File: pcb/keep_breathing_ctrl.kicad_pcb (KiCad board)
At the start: 4 copper layers, 131 x 112 mm, 149 parts, among them J1 Barrel_Jack_Switch, J2 Screw_Terminal, P1 CONN_RASPBERRY, Q1 PN2222, Q2 PN2222, U1 MPL3115A2, U10 PCF8523TK, U11 AQH3213AX, U12 AQH3213AX, U13 HTS221, U14 ICE40UP5K-SG48ITR, U15 W25Q32JVSSIM, U16 UCC12040, U17 ISO7762, U2 powerSTEP01, U3 TLP240D, U4 TLP240D, U5 TLP240D, U6 TLP240D, U7 TLP240D, U8 TLP240D, U9 ZLDO1117G33TA

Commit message: stepper planes
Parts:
- C43, C46, C49, C51, C52, C53, R30: moved to B.Cu
- moved C46 168.6 mm to (142.7, 91.4)
- moved C53 144.0 mm to (127.3, 94.7)
- moved C43 143.4 mm to (139.7, 91.9)
- moved C52 140.3 mm to (127.4, 92.7)
- moved U15 138.6 mm to (124.5, 87.9)
- moved C51 137.0 mm to (134.5, 81.4)
- moved C49 135.4 mm to (134.8, 83.5)
- moved R30 133.6 mm to (127.5, 88.7), turned to 180 degrees
- moved R4 9.93 mm to (63.0, 106.6), turned to 90 degrees
- moved C9 7.27 mm to (56.5, 131.0)
- moved C5 6.79 mm to (61.2, 106.6), turned to 90 degrees
- moved C4 0.62 mm to (59.5, 123.3)
- moved C12 0.51 mm to (59.5, 121.5)
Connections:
- C42 pad 1: /SensorShields/+1.2V_CORE -> +1V2
- R32 pad 2: (no net) -> +1V2
- U14 pad 30: /SensorShields/+1.2V_CORE -> +1V2
- U14 pad 5: /SensorShields/+1.2V_CORE -> +1V2
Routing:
- net GND_MOTOR: track 1.65 -> 8.69 mm, vias 42 -> 46
- net SM_ADC: track 16.1 -> 16.7 mm
- net OUTA1: track 6.04 -> 6.29 mm, vias 14 -> 15
- net OUTB1: vias 14 -> 15
- added copper zone on F.Cu, net GND_MOTOR
- added copper zone on In2.Cu, net GND_MOTOR
- added copper zone on F.Cu, net VMOTOR
- added copper zone on In1.Cu, net VMOTOR
- removed copper zone on F.Cu, net GND

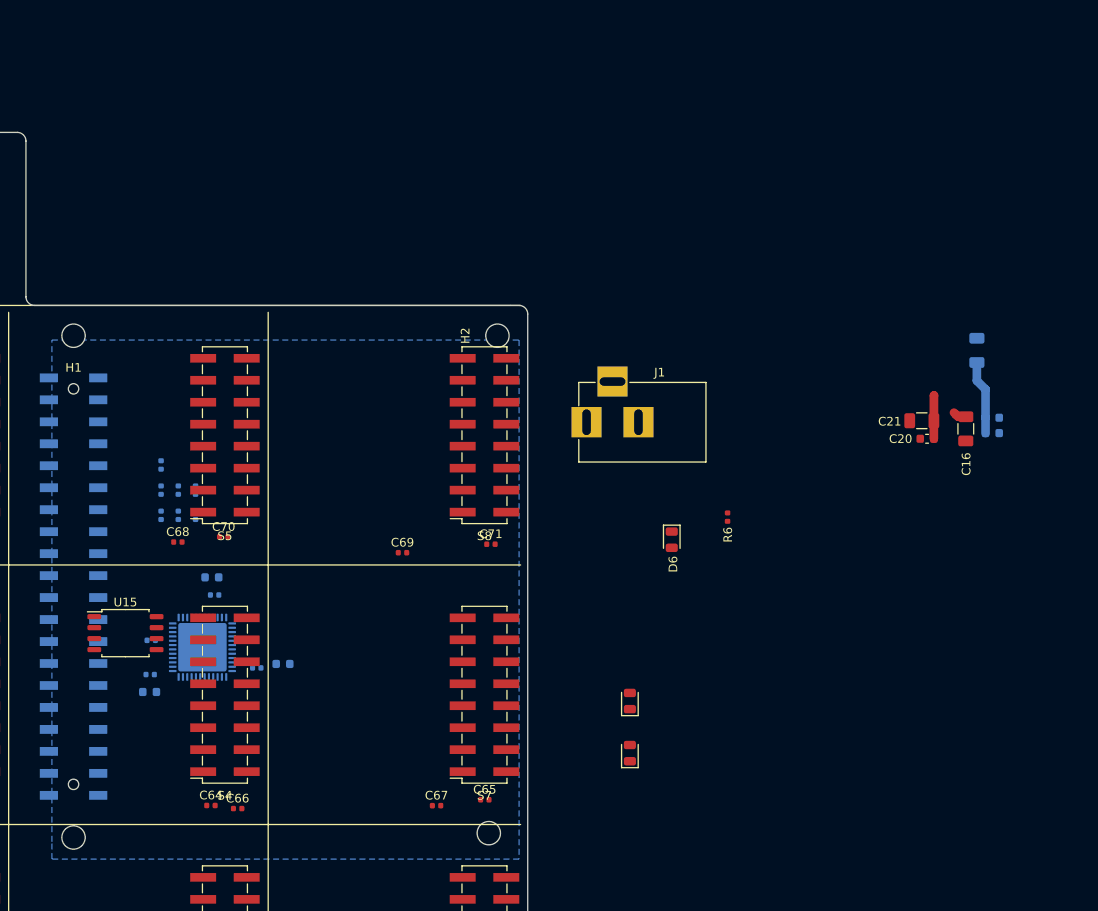
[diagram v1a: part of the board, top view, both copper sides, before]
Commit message: stm32 jtag  connected
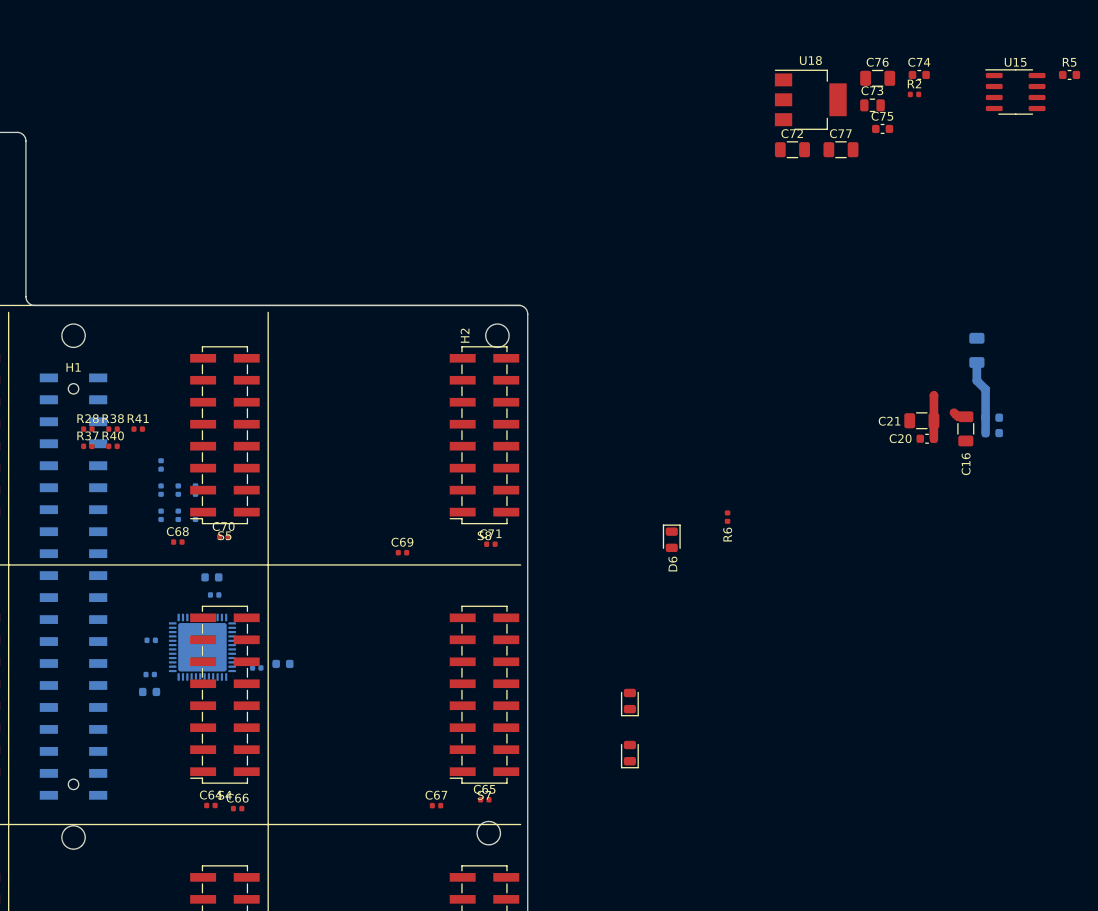
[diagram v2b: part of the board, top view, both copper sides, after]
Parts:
- removed J1: Barrel_Jack_Switch, TH:BARREL_JACK
- added C72: 33u, Capacitor_SMD:C_1206_3216Metric, F.Cu at (201.6, 32.0)
- added C73: 10u, Capacitor_SMD:C_0805_2012Metric, F.Cu at (210.8, 26.9)
- added C74: 0.1u, Capacitor_SMD:C_0603_1608Metric, F.Cu at (216.3, 23.4)
- added C75: 0.1u, Capacitor_SMD:C_0603_1608Metric, F.Cu at (212.0, 29.6)
- added C76: 33u, Capacitor_SMD:C_1206_3216Metric, F.Cu at (211.4, 23.8)
- added C77: 33u, Capacitor_SMD:C_1206_3216Metric, F.Cu at (207.2, 32.0)
- added R2: 120, Resistor_SMD:R_0402_1005Metric, F.Cu at (215.7, 25.6)
- added R28: 100, Resistor_SMD:R_0402_1005Metric, F.Cu at (120.2, 64.3)
- added R37: 100, Resistor_SMD:R_0402_1005Metric, F.Cu at (120.2, 66.3)
- added R38: 100, Resistor_SMD:R_0402_1005Metric, F.Cu at (123.1, 64.3)
- added R40: 100, Resistor_SMD:R_0402_1005Metric, F.Cu at (123.1, 66.3)
- added R41: 100, Resistor_SMD:R_0402_1005Metric, F.Cu at (126.0, 64.3)
- added R5: 10K, Resistor_SMD:R_0603_1608Metric, F.Cu at (233.6, 23.4)
- added U18: ZLDO1117G33TA, SMD:SOT-223, F.Cu at (203.7, 26.2)
- U15: value W25Q32JVSSIM -> GD25Q32CTIGR-Memory_Flash; footprint Package_SO:SOIC-8_5.23x5.23mm_P1.27mm -> Package_SO:SOIC-8_3.9x4.9mm_P1.27mm
- moved U15 120.4 mm to (227.4, 25.3)
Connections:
- net +1V2 renamed 1V2_ICE
- C20 pad 1: 3V3_ESP -> 3V3_STM
- C21 pad 1: 3V3_ESP -> 3V3_STM
- C43 pad 1: +3V3 -> 3V3_ICE
- C44 pad 1: +3V3 -> 3V3_ICE
- C45 pad 1: +3V3 -> 3V3_ICE
- C46 pad 1: +3V3 -> 3V3_ICE
- C49 pad 1: +3V3 -> 3V3_ICE
- C51 pad 1: +3V3 -> 3V3_ICE
- C52 pad 1: +3V3 -> 3V3_ICE
- C53 pad 1: +3V3 -> 3V3_ICE
- P1 pad 12: (no net) -> /Rapsberry/JNRST
- P1 pad 16: (no net) -> /Rapsberry/JTDO
- P1 pad 18: (no net) -> /Rapsberry/JTDI
- P1 pad 19: (no net) -> /Rapsberry/SPI_MOSI
- P1 pad 21: (no net) -> /Rapsberry/SPI_MISO
- P1 pad 22: (no net) -> /Rapsberry/JTCK
- P1 pad 23: (no net) -> /Rapsberry/SPI_CLK
- P1 pad 24: (no net) -> /Rapsberry/SPI_CS
- P1 pad 26: (no net) -> /Rapsberry/JTMS
- P1 pad 29: (no net) -> /Rapsberry/RST_ICE
- R29 pad 2: +3V3 -> 3V3_ICE
- R30 pad 2: +3V3 -> 3V3_ICE
- R31 pad 2: +3V3 -> 3V3_ICE
- R33 pad 2: +3V3 -> 3V3_ICE
- R34 pad 2: +3V3 -> 3V3_ICE
- U14 pad 1: +3V3 -> 3V3_ICE
- U14 pad 14: (no net) -> /SensorShields/FPGA_SO
- U14 pad 17: (no net) -> /SensorShields/FPGA_SI
- U14 pad 22: +3V3 -> 3V3_ICE
- U14 pad 33: +3V3 -> 3V3_ICE
- U15 pad 2: (no net) -> /SensorShields/FPGA_SI
- U15 pad 5: (no net) -> /SensorShields/FPGA_SO
- U15 pad 8: +3V3 -> 3V3_ICE
- U9 pad 2: 3V3_ESP -> 3V3_STM
- U9 pad 4: 3V3_ESP -> 3V3_STM
- UST1 pad 100: +3.3VP -> 3V3_STM
- UST1 pad 11: +3.3VP -> 3V3_STM
- UST1 pad 19: +3.3VP -> 3V3_STM
- UST1 pad 28: +3.3VP -> 3V3_STM
- UST1 pad 50: +3.3VP -> 3V3_STM
- UST1 pad 72: (no net) -> /Rapsberry/JTMS
- UST1 pad 75: +3.3VP -> 3V3_STM
- UST1 pad 76: (no net) -> /Rapsberry/JTCK
- UST1 pad 77: (no net) -> /Rapsberry/JTDI
- UST1 pad 89: (no net) -> /Rapsberry/JTDO
- UST1 pad 90: (no net) -> /Rapsberry/JNRST
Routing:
- net 3V3_STM: track 0.00 -> 5.03 mm
- net 3V3_ESP: track 5.03 -> 0.00 mm
- removed copper zone on B.Cu, net GND

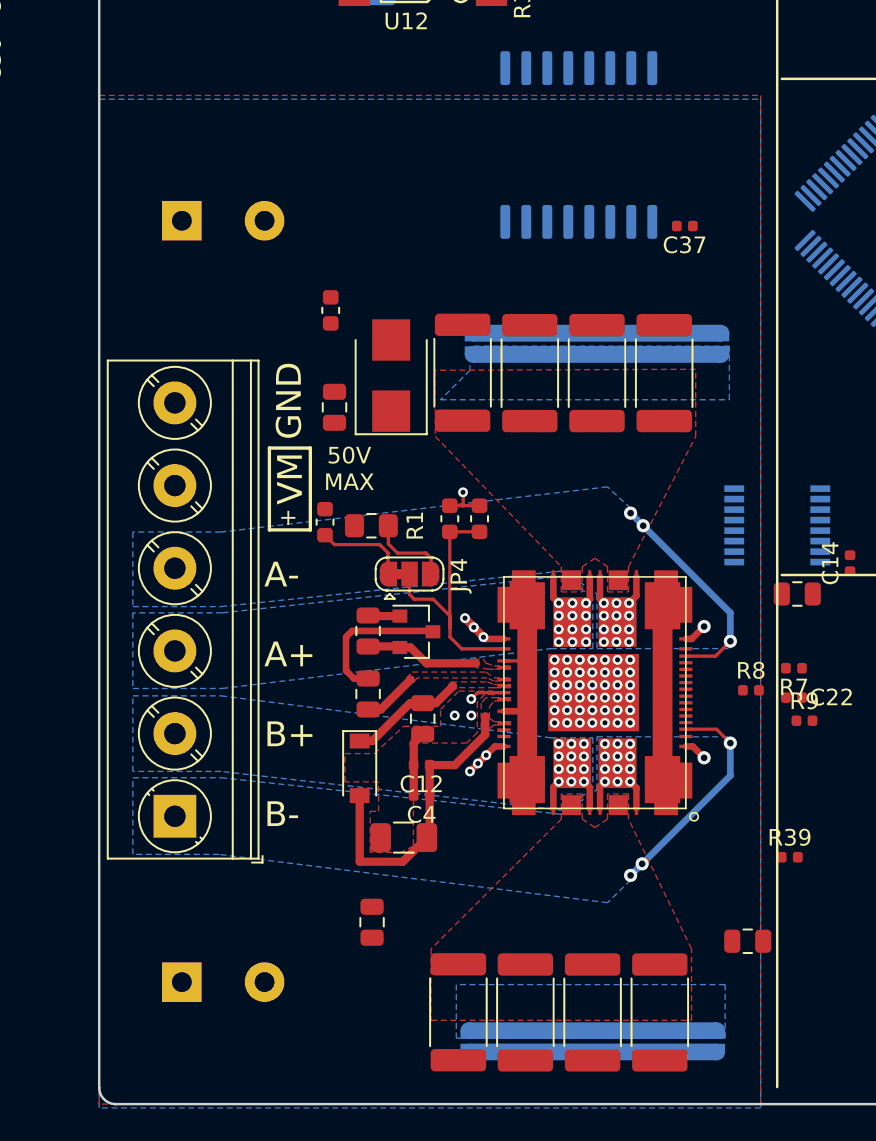
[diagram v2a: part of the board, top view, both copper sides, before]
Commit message: GND for motor driver
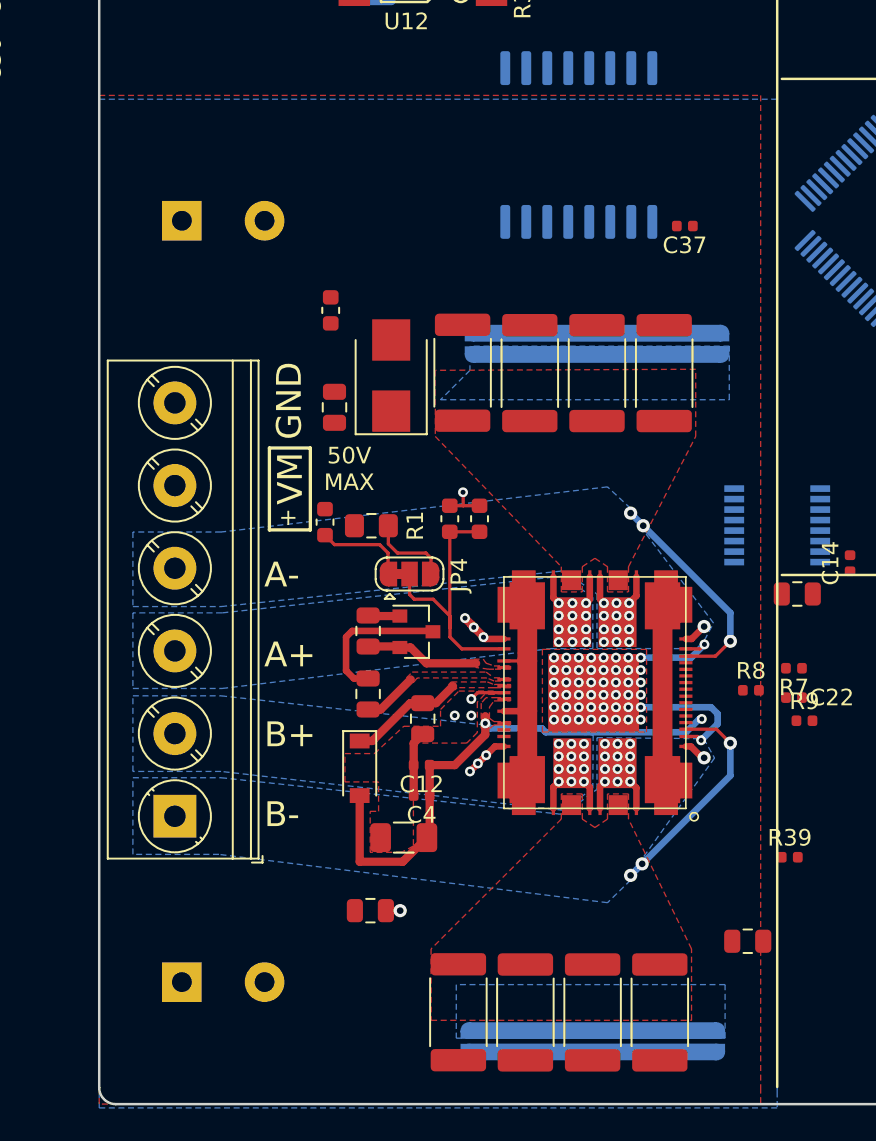
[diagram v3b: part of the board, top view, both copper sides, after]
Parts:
- moved C9 0.71 mm to (56.4, 130.3), turned to 0 degrees
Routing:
- net GND_MOTOR: track 8.69 -> 22.8 mm, vias 46 -> 55
- net 3V3_M: track 18.4 -> 32.0 mm, vias 0 -> 2

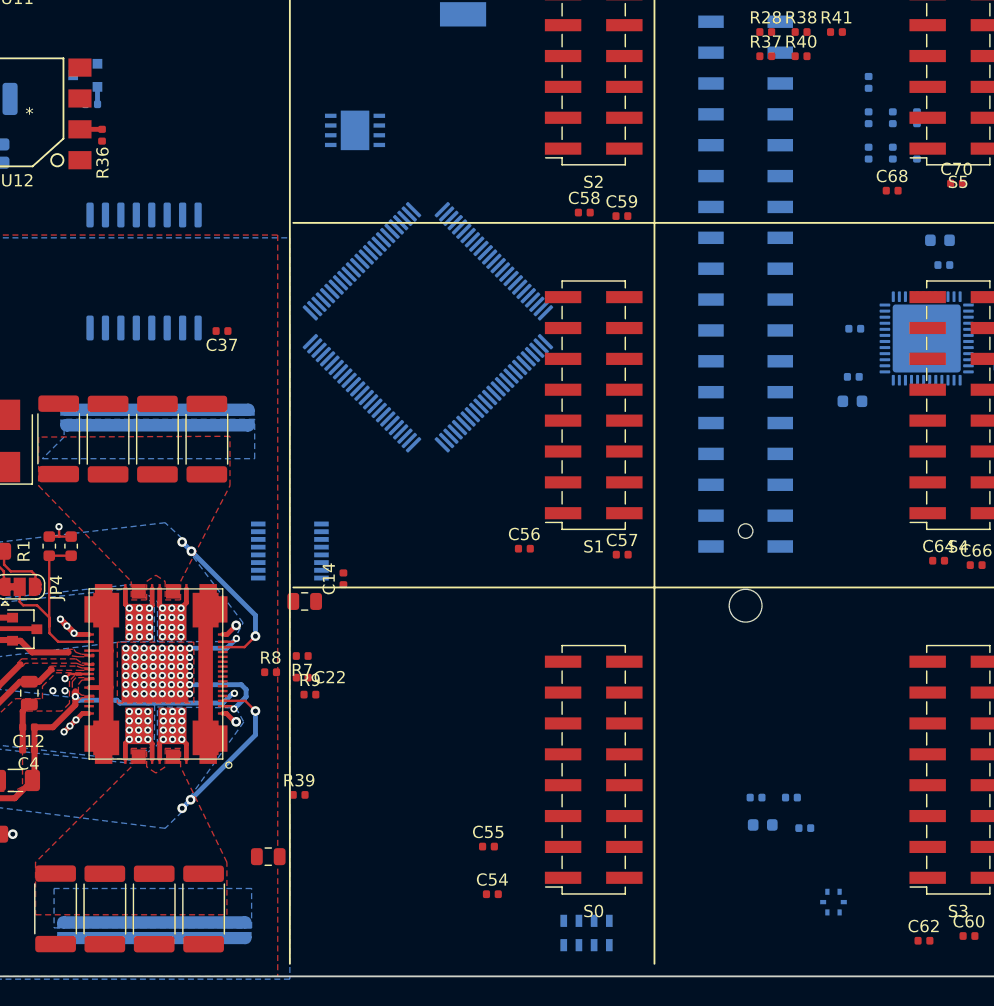
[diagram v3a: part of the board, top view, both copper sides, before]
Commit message: rtc placement
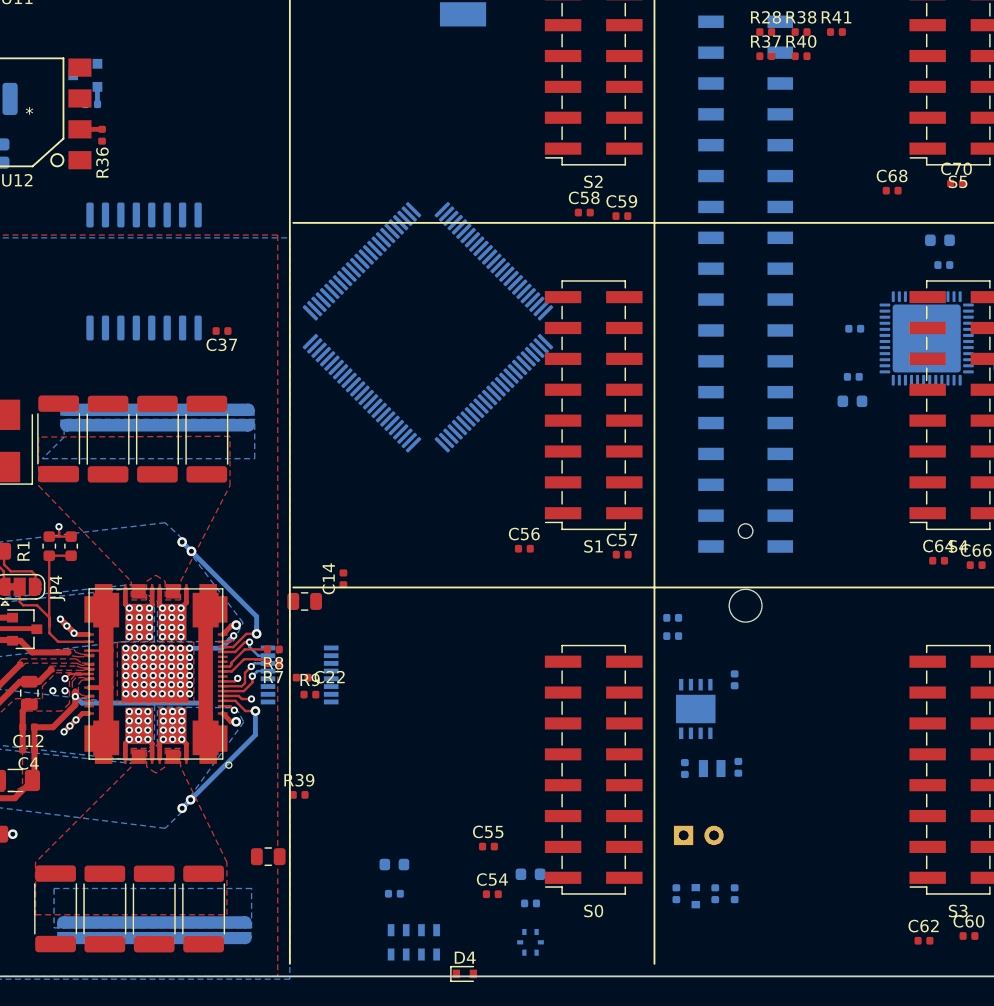
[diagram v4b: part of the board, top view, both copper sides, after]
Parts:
- added C24: JUWT1105MCD, Capacitor_THT:CP_Radial_D6.3mm_P2.50mm, B.Cu at (113.4, 130.4)
- added D4: 1N4148WT-7, Diode_SMD:D_SOD-523, F.Cu at (95.4, 141.8)
- added D7: 1SS389,L3F, Diode_SMD:D_SOD-523, B.Cu at (114.4, 135.4)
- added R13: 100, Resistor_SMD:R_0402_1005Metric, B.Cu at (112.8, 135.2)
- added Y1: ABS06-107-32.768KHZ-T, SMD:ABS06-107, B.Cu at (115.8, 124.9)
- C32: value 100nF -> 10uF; footprint Capacitor_SMD:C_0402_1005Metric -> Capacitor_SMD:C_0603_1608Metric
- moved R12 65.5 mm to (116.0, 135.2)
- moved R10 62.8 mm to (117.6, 135.2), turned to 90 degrees
- moved U10 55.3 mm to (114.4, 120.0), turned to 180 degrees
- moved C23 52.8 mm to (113.5, 124.9)
- moved C25 52.1 mm to (117.9, 124.8), turned to 90 degrees
- moved R14 48.3 mm to (112.5, 114.0), turned to 180 degrees
- moved C26 47.5 mm to (117.6, 117.6)
- moved R15 45.8 mm to (112.5, 112.5), turned to 180 degrees
- moved C15 30.8 mm to (89.6, 135.2)
- moved C41 30.5 mm to (89.6, 132.8)
- moved U13 25.1 mm to (100.8, 139.2)
- moved C31 23.4 mm to (100.8, 136.0)
- moved C32 22.4 mm to (100.8, 133.6)
- moved U1 14.2 mm to (91.2, 139.2)
- moved U17 10.2 mm to (81.8, 117.2)
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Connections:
- U10 pad 3: (no net) -> Net-(C24-Pad1)
- U17 pad 12: /Power Stepper/SM_SI -> /Power Stepper/SM_CS
- U17 pad 14: /Power Stepper/SM_RST -> /Power Stepper/SM_SI
- U17 pad 15: /Power Stepper/SM_CS -> /Power Stepper/SM_RST
- U17 pad 3: (no net) -> /Power Stepper/M_MOSI
- U17 pad 5: /Power Stepper/M_MOSI -> (no net)
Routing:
- net GND_MOTOR: track 22.8 -> 15.9 mm
- net /Power Stepper/SM_SI: track 0.00 -> 5.00 mm, vias 0 -> 1
- net /Power Stepper/SM_RST: track 0.00 -> 4.75 mm, vias 0 -> 1
- net SM_BUSY: track 0.00 -> 4.72 mm
- net /Power Stepper/SM_CLK: track 0.00 -> 4.72 mm, vias 0 -> 1
- net SM_FLAG: track 0.00 -> 4.36 mm
- net /Power Stepper/SM_CS: track 0.00 -> 2.47 mm, vias 0 -> 1
- net 3V3_M: track 32.0 -> 30.6 mm
